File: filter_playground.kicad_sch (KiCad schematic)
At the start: 18 parts, among them J1 Filter, J11 SDR ANT, J2 Filter, Q4 2N7002, Q5 2N7002, U11 74LVC1G3157GW, U14 74LVC1G3157GW, U18 74LVC1G3157GW

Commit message: Fixing lots of schematic issues
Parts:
- added C10, C11, C13, C68: 100nF, PCM_JLCPCB:C_0402, symbol PCM_JLCPCB-Capacitors:0402,100nF,(2)
- added R77, R78: 10kΩ, PCM_JLCPCB:R_0402, symbol PCM_JLCPCB-Resistors:0402,10kΩ
- U11, U14, U18: footprint (none) -> PCM_JLCPCB:SOT-363_SC-70-6
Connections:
- net +3.3VA is gone; now on net VDDA: R42.1, R43.1
- net at J2.1 (Pin_1): now also C11.2; no longer U11.3
- net at J2.4 (Pin_4): now also C68.1; no longer U14.3
- net at C6.2, U11.4: now also R78.2
- net at U11.1: now also C10.1; no longer J1.1 (Pin_1)
- net at U14.4, U18.4: now also R77.2
- net at J1.4 (Pin_4): now also C13.1; no longer U14.1
- new net: C13.2, U14.1
- new net: C68.2, U14.3
- new net: C11.1, U11.3
- new net: C10.2, J1.1 (Pin_1)
- new net VA/2: R77.1, R78.1
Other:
- moved on the sheet: C14, C6, J1, J11, J2, Q5, R43, TR1, U11A

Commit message: Fixed a lot more mistakes...
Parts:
- added C104, C105: 100nF, PCM_JLCPCB:C_0402, symbol PCM_JLCPCB-Capacitors:0402,100nF,(2)
- TP10, TP12: footprint TP_Label:TestPoint_THTPad_D2.0mm_Drill1.0mm -> TestPoint:TestPoint_THTPad_D2.5mm_Drill1.2mm
- U11, U14, U18: Price (none) -> $0.09
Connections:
- net RX_OUT: now also C105.2; no longer U18.3
- net TX_OUT: now also C104.2; no longer U18.1
- net at J11.1 (In): now also C14.1
- new net: C105.1, U18.3
- new net: C104.1, U18.1
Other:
- moved on the sheet: C14, J11

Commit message: Starting to place components
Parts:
- C14: footprint PCM_JLCPCB:C_0805 -> PCM_JLCPCB:C_0402; symbol PCM_JLCPCB-Capacitors:0805,100nF -> PCM_JLCPCB-Capacitors:0402,100nF,(2); LCSC C28233 -> C307331; Manufacturer (none) -> Samsung Electro-Mechanics; Part CL21B104KCFNNNE -> CL05B104KB54PNC; Price 0.009USD -> 0.008USD; Stock 1168020 -> 8389599; Voltage Rated 100V -> 50V
- J1, J2: footprint (none) -> Connector_PinSocket_2.54mm:PinSocket_1x04_P2.54mm_Vertical
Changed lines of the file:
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@@
 			)
 		)
-		(property "Footprint" ""
+		(property "Footprint" "Connector_PinSocket_2.54mm:PinSocket_1x04_P2.54mm_Vertical"
 			(at 115.57 82.55 0)
 			(hide yes)
@@
 		)
 		(property "Voltage Rated" "50V"
-			(at 203.2 63.5 90)
+			(at 205.2462 65.278 0)
 			(show_name no)
 			(do_not_autoplace no)
@@
 					(size 0.8 0.8)
 				)
+				(justify left)
 			)
 		)
@@
 		)
 		(property "Voltage Rated" "50V"
-			(at 123.952 160.528 0)
+			(at 129.032 160.7962 0)
 			(show_name no)
 			(do_not_autoplace no)
@@
 		)
 		(property "Voltage Rated" "50V"
-			(at 128.27 81.28 90)
+			(at 130.3162 79.502 0)
 			(show_name no)
 			(do_not_autoplace no)
@@
 					(size 0.8 0.8)
 				)
+				(justify left)
 			)
 		)
@@
 		)
 		(property "Voltage Rated" "50V"
-			(at 99.822 161.798 0)
+			(at 104.902 162.0662 0)
 			(show_name no)
 			(do_not_autoplace no)
@@
 			)
 		)
-		(property "Footprint" ""
+		(property "Footprint" "Connector_PinSocket_2.54mm:PinSocket_1x04_P2.54mm_Vertical"
 			(at 115.57 62.23 0)
 			(hide yes)
@@
 		)
 		(property "Voltage Rated" "50V"
-			(at 203.2 81.28 90)
+			(at 205.2462 79.502 0)
 			(show_name no)
 			(do_not_autoplace no)
@@
 					(size 0.8 0.8)
 				)
+				(justify left)
 			)
 		)
@@
 	)
 	(symbol
-		(lib_id "PCM_JLCPCB-Capacitors:0805,100nF")
+		(lib_id "PCM_JLCPCB-Capacitors:0402,100nF,(2)")
 		(at 39.37 72.39 90)
 		(unit 1)
@@
 			)
 		)
-		(property "Footprint" "PCM_JLCPCB:C_0805"
+		(property "Footprint" "PCM_JLCPCB:C_0402"
 			(at 39.37 74.168 90)
 			(hide yes)
@@
 			)
 		)
-		(property "Datasheet" "https://www.lcsc.com/datasheet/lcsc_datasheet_2304140030_Samsung-Electro-Mechanics-CL21B104KCFNNNE_C28233.pdf"
+		(property "Datasheet" "https://www.lcsc.com/datasheet/lcsc_datasheet_2304140030_Samsung-Electro-Mechanics-CL05B104KB54PNC_C307331.pdf"
 			(at 39.37 72.39 0)
 			(hide yes)
@@
 			)
 		)
-		(property "Description" "100V 100nF X7R ±10% 0805 Multilayer Ceramic Capacitors MLCC - SMD/SMT ROHS"
+		(property "Description" "50V 100nF X7R ±10% 0402 Multilayer Ceramic Capacitors MLCC - SMD/SMT ROHS"
 			(at 39.37 72.39 0)
 			(hide yes)
@@
 			)
 		)
-		(property "LCSC" "C28233"
+		(property "LCSC" "C307331"
 			(at 39.37 72.39 0)
 			(hide yes)
@@
 			)
 		)
-		(property "Stock" "1168020"
+		(property "Stock" "8389599"
 			(at 39.37 72.39 0)
 			(hide yes)
@@
 			)
 		)
-		(property "Price" "0.009USD"
+		(property "Price" "0.008USD"
 			(at 39.37 72.39 0)
 			(hide yes)
@@
 			)
 		)
-		(property "Part" "CL21B104KCFNNNE"
+		(property "Part" "CL05B104KB54PNC"
 			(at 39.37 72.39 0)
 			(hide yes)
@@
 			)
 		)
-		(property "Voltage Rated" "100V"
+		(property "Voltage Rated" "50V"
 			(at 39.37 68.58 90)
 			(show_name no)
@@
 			)
 		)
+		(property "Manufacturer" "Samsung Electro-Mechanics"
+			(at 39.37 72.39 0)
+			(hide yes)
+			(show_name no)
+			(do_not_autoplace no)
+			(effects
+				(font
+					(size 1.27 1.27)
+				)
+			)
+		)
 		(pin "2"
 		)
@@
 		)
 		(property "Voltage Rated" "50V"
-			(at 74.422 161.798 0)
+			(at 79.502 162.0662 0)
 			(show_name no)
 			(do_not_autoplace no)
@@
 		)
 		(property "Voltage Rated" "50V"
-			(at 105.41 81.28 90)
+			(at 107.4562 79.502 0)
 			(show_name no)
 			(do_not_autoplace no)
@@
 					(size 0.8 0.8)
 				)
+				(justify left)
 			)
 		)

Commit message: AF DAC Some VDDA Placed
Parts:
- added R82, R83, R85, R86: 100kΩ, PCM_JLCPCB:R_0402, symbol PCM_JLCPCB-Resistors:0402,100kΩ
- TR4: renamed from TR1; footprint Intro_to_CAD:XFMR_H1102NLT -> Transformer_SMD:Transformer_Ethernet_Wuerth_749013011A
- renumbered C76 to C100, C13 to C101, C68 to C102, C75 to C103, C105 to C104, C104 to C105, C14 to C95, C6 to C96, C77 to C97, C10 to C98, C11 to C99, J11 to J10, J1 to J11, J2 to J12, Q5 to Q8, Q4 to Q9, R78 to R81, R43 to R84, R77 to R87, R42 to R88, TP10 to TP12, TP12 to TP13, U11 to U22, U14 to U23, U18 to U24
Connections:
- net VA/2: now also R82.1, R83.1, R85.1, R86.1
- net at C101.2, U23.1: now also R85.2
- net at C102.2, U23.3: now also R86.2
- net at C98.1, U22.1: now also R82.2
- net at C99.1, U22.3: now also R83.2
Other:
- moved on the sheet: C100, C101, C102, C103, C97, U22B, U23B, U24B

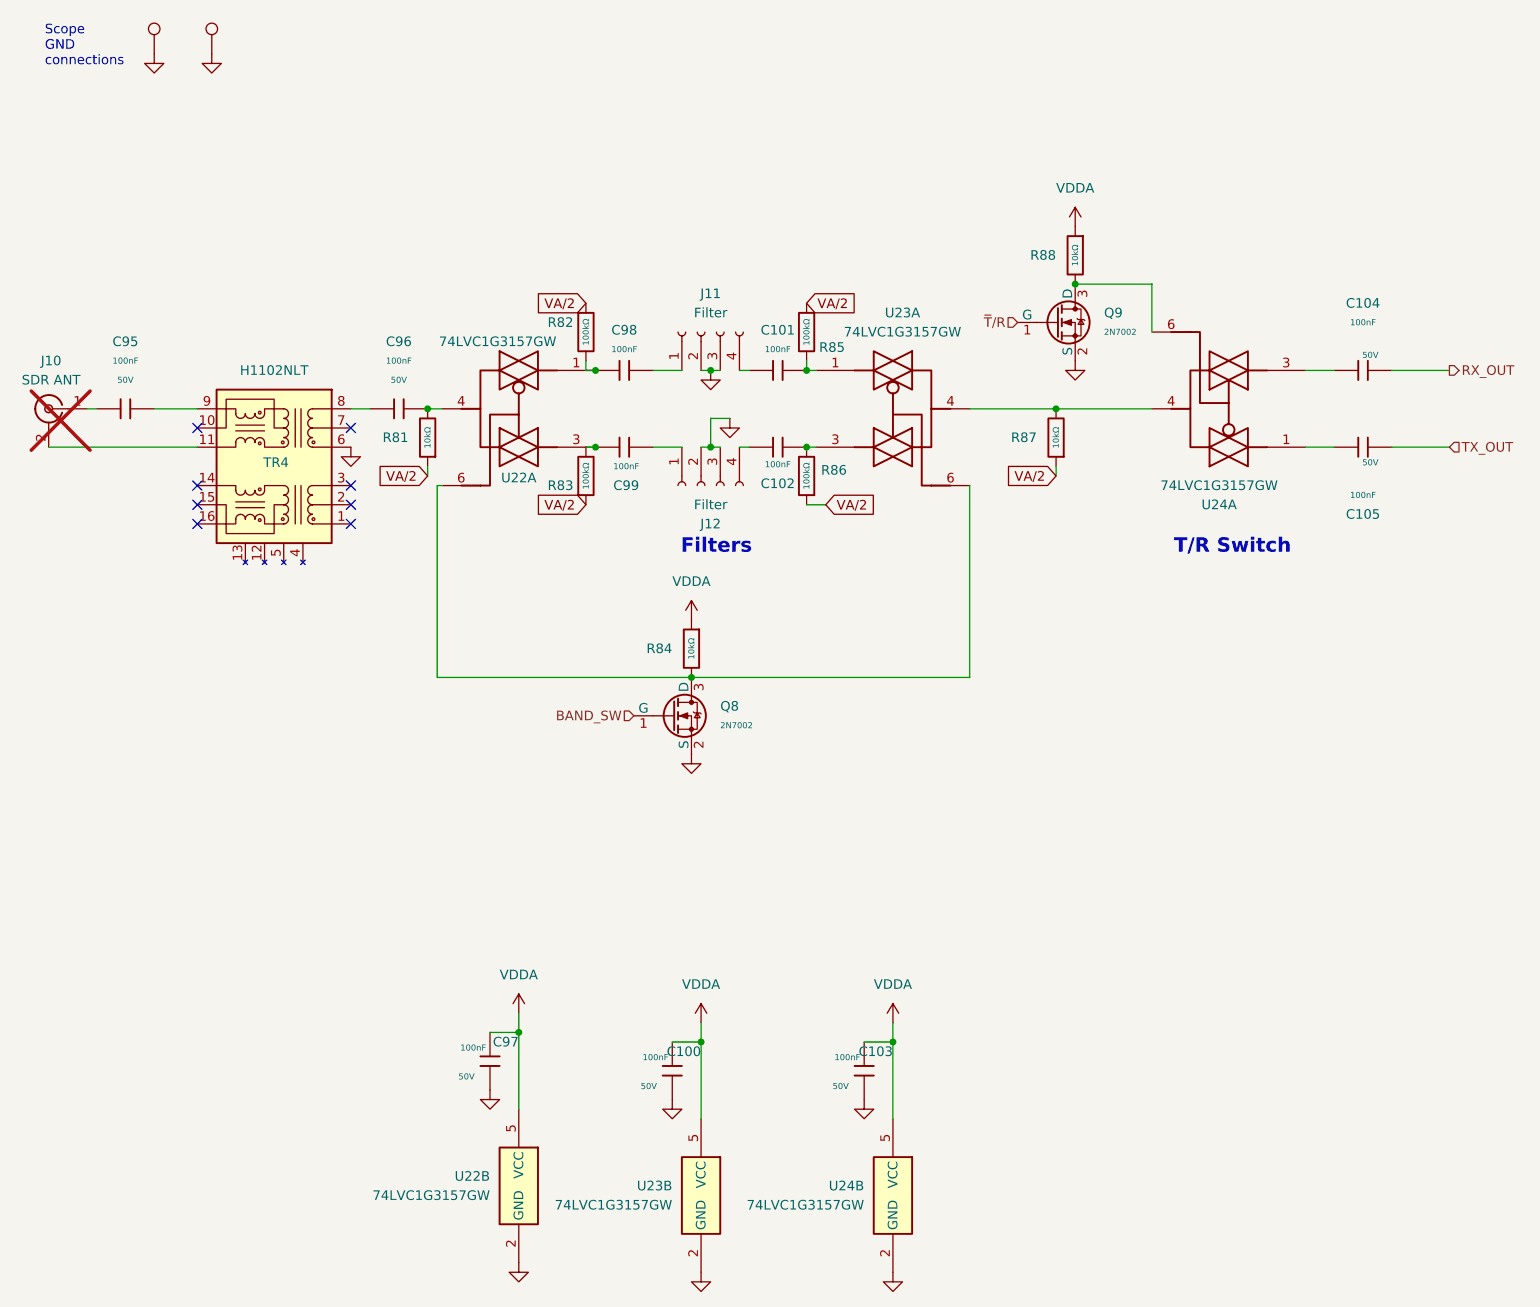
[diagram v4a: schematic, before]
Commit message: Fixed schematic errors, all placed
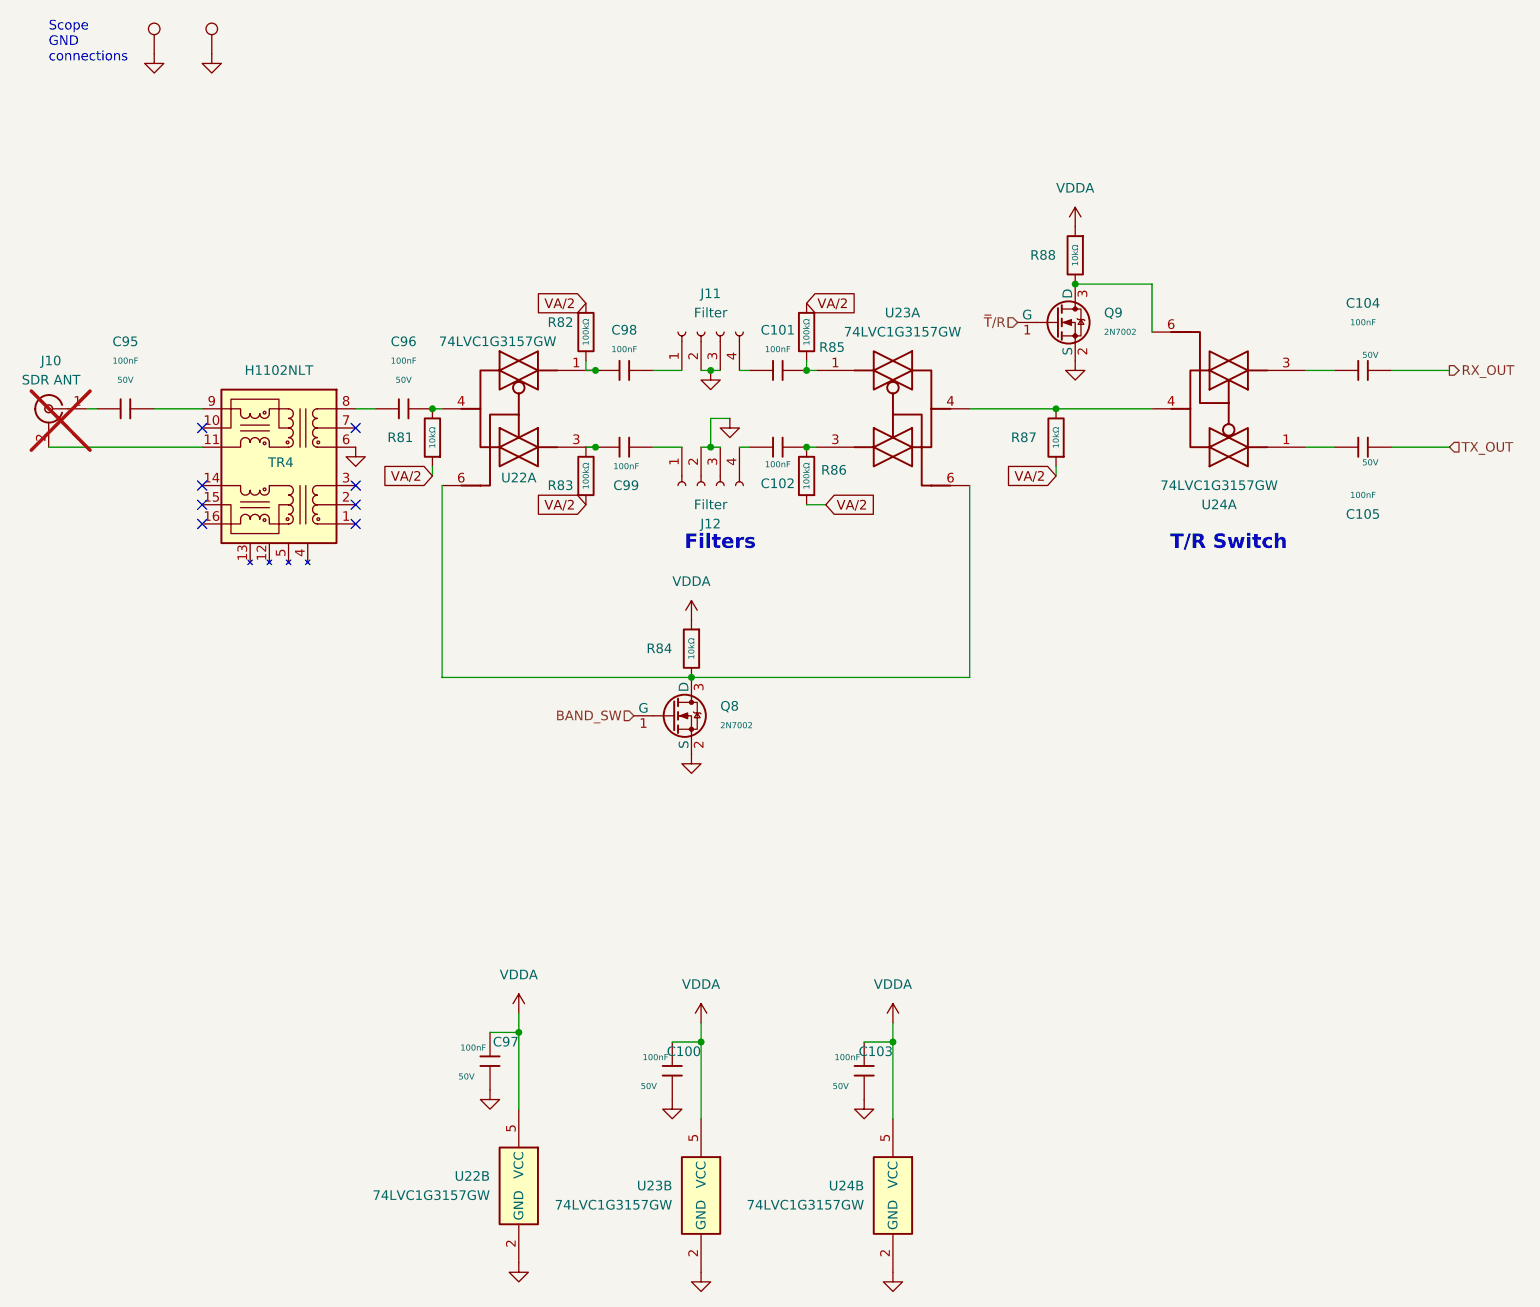
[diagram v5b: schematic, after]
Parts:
- Q8, Q9: symbol JLCPCB-Transistors:NMOS,2N7002 -> PCM_JLCPCB-Transistors:NMOS,2N7002K; Attrition Qty 5 -> 4; Category Transistors,MOSFETs -> Triode/MOS Tube/Transistor,MOSFETs; Class Basic Component -> Preferred Component; LCSC C8545 -> C22379475; Manufacturer Changjiang Electronics Tech (CJ) -> hongjiacheng; Part 2N7002 -> 2N7002K; Stock 1078050 -> 82639
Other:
- moved on the sheet: C96, R81, TR4

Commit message: Added test points
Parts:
- added TP17, TP18: GND, TestPoint:TestPoint_THTPad_D2.5mm_Drill1.2mm, symbol Connector:TestPoint
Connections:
- net GND: now also TP17.1, TP18.1

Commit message: Added Prototype Area
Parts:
- TP12, TP13, TP17, TP18: footprint TestPoint:TestPoint_THTPad_D2.5mm_Drill1.2mm -> RP2040_minimal:TestPoint_THTPad_D2.5mm_Drill1.2mm
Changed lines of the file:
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@@
 			)
 		)
-		(property "Footprint" "TestPoint:TestPoint_THTPad_D2.5mm_Drill1.2mm"
+		(property "Footprint" "RP2040_minimal:TestPoint_THTPad_D2.5mm_Drill1.2mm"
 			(at 71.12 25.4 0)
 			(hide yes)
@@
 			)
 		)
-		(property "Footprint" "TestPoint:TestPoint_THTPad_D2.5mm_Drill1.2mm"
+		(property "Footprint" "RP2040_minimal:TestPoint_THTPad_D2.5mm_Drill1.2mm"
 			(at 63.5 25.4 0)
 			(hide yes)
@@
 			)
 		)
-		(property "Footprint" "TestPoint:TestPoint_THTPad_D2.5mm_Drill1.2mm"
+		(property "Footprint" "RP2040_minimal:TestPoint_THTPad_D2.5mm_Drill1.2mm"
 			(at 48.26 25.4 0)
 			(hide yes)
@@
 			)
 		)
-		(property "Footprint" "TestPoint:TestPoint_THTPad_D2.5mm_Drill1.2mm"
+		(property "Footprint" "RP2040_minimal:TestPoint_THTPad_D2.5mm_Drill1.2mm"
 			(at 55.88 25.4 0)
 			(hide yes)

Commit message: Some 3D models
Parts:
- J10: now fitted
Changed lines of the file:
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@@
 		(on_board yes)
 		(in_pos_files yes)
-		(dnp yes)
+		(dnp no)
 		(property "Reference" "J10"
 			(at 29.5274 66.04 0)
